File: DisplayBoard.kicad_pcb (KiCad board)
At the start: 4 copper layers, 35.6 x 38.2 mm, 42 parts, among them J201 Conn_Coaxial, J301 Conn_01x12_Pin, J401 Conn_01x04, Q301 L2N7002SLLT1G, U201 ESP32-S3-PICO-1-N8R2, U401 SN65HVD232, U501 USBLC6-2SC6, U502 AMS1117-3.3

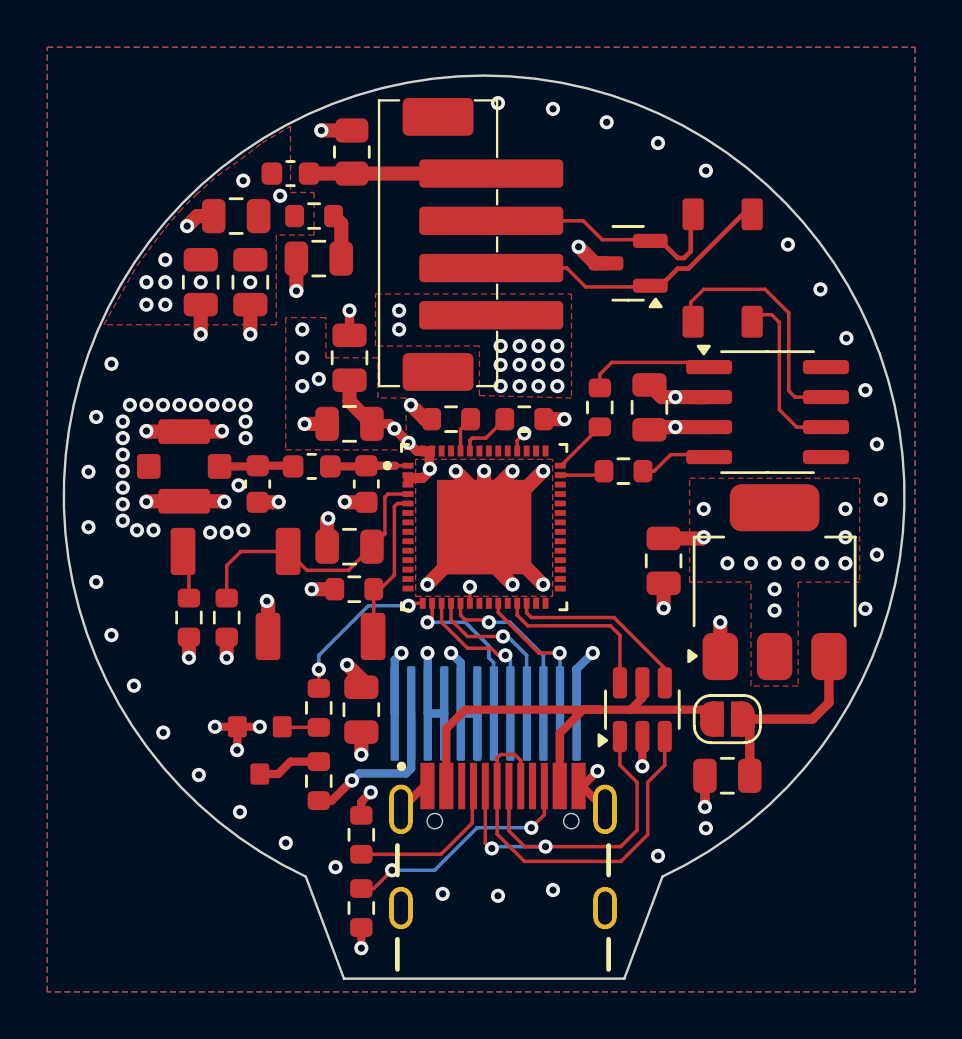
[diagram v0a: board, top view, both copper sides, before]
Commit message: Fixed wrong board outlines
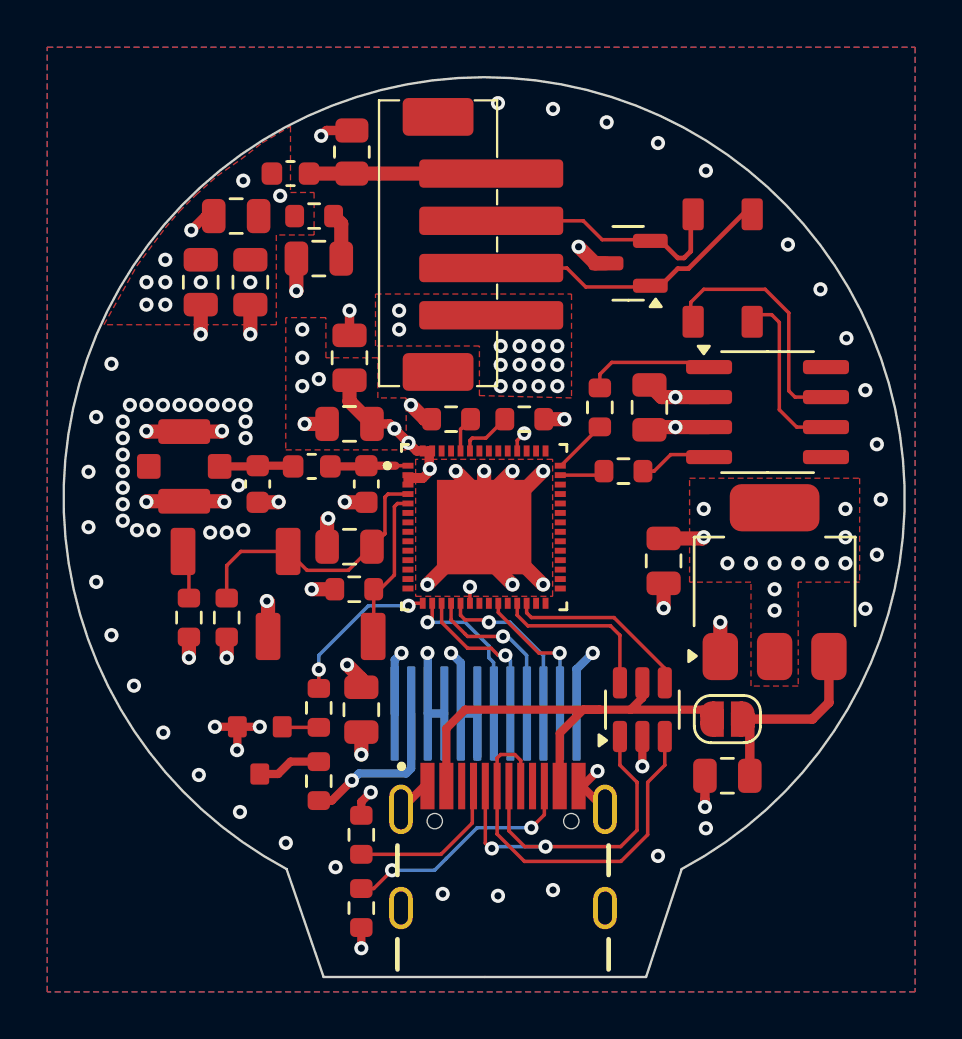
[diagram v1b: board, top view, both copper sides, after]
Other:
- board size 35.6 x 38.2 mm -> 35.6 x 38.1 mm
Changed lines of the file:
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@@
 		(embedded_fonts no)
 	)
+	(gr_line
+		(start 91.634396 133.548783)
+		(end 93.203009 138.119579)
+		(stroke
+			(width 0.1)
+			(type solid)
+		)
+		(layer "Edge.Cuts")
+	)
 	(gr_arc
-		(start 92.449248 133.869123)
-		(mid 100.000001 99.950001)
-		(end 107.55075 133.869124)
+		(start 91.634396 133.548783)
+		(mid 100 100.019548)
+		(end 108.365604 133.548783)
 		(stroke
 			(width 0.1)
@@
 	)
 	(gr_line
-		(start 94.06443 138.189125)
-		(end 105.935567 138.189126)
+		(start 106.858009 138.119579)
+		(end 108.365604 133.548783)
 		(stroke
 			(width 0.1)
@@
 	)
 	(gr_line
-		(start 92.449248 133.869123)
-		(end 94.06443 138.189125)
+		(start 100.033009 138.119579)
+		(end 106.858009 138.119579)
 		(stroke
 			(width 0.1)
@@
 	)
 	(gr_line
-		(start 107.55075 133.869124)
-		(end 105.935567 138.189126)
+		(start 100.033009 138.119579)
+		(end 93.203009 138.119579)
 		(stroke
 			(width 0.1)
@@
 	)
 	(segment
-		(start 87.848272 105.9)
-		(end 87.424641 106.323631)
-		(width 0.6)
-		(layer "F.Cu")
-		(net 1)
-	)
-	(segment
 		(start 100 119.069563)
 		(end 101.059563 119.069563)
@@
 	)
 	(segment
+		(start 94.4 102.275)
+		(end 93.325 102.275)
+		(width 0.4)
+		(layer "F.Cu")
+		(net 1)
+	)
+	(segment
 		(start 109.35 130.616687)
 		(end 109.352521 130.619208)
@@
 	)
 	(segment
-		(start 88.55 105.9)
-		(end 87.848272 105.9)
-		(width 0.6)
-		(layer "F.Cu")
-		(net 1)
-	)
-	(segment
 		(start 109.35 129.6)
 		(end 109.35 130.916687)
@@
 	)
 	(segment
-		(start 94.4 102.275)
-		(end 93.107902 102.275)
-		(width 0.6)
-		(layer "F.Cu")
-		(net 1)
-	)
-	(segment
 		(start 104.135 130.034999)
 		(end 105.120001 131.02)
@@
 	)
 	(segment
+		(start 93.325 102.275)
+		(end 93.1 102.5)
+		(width 0.4)
+		(layer "F.Cu")
+		(net 1)
+	)
+	(segment
 		(start 100 119.069563)
 		(end 100 119.1)
@@
 	)
 	(segment
-		(start 93.107902 102.275)
-		(end 93.107893 102.274991)
-		(width 0.6)
+		(start 88.55 105.9)
+		(end 88.2 105.9)
+		(width 0.4)
 		(layer "F.Cu")
 		(net 1)
@@
 	)
 	(segment
+		(start 88.2 105.9)
+		(end 87.6 106.5)
+		(width 0.4)
+		(layer "F.Cu")
+		(net 1)
+	)
+	(segment
 		(start 89.55 127.525)
 		(end 89.55 128.500995)
@@
 	)
 	(via
-		(at 85.7 113.9)
+		(at 87.6 106.5)
 		(size 0.6)
 		(drill 0.3)
@@
 	)
 	(via
-		(at 89.661103 131.133185)
+		(at 85.7 113.9)
 		(size 0.6)
 		(drill 0.3)
@@
 	)
 	(via
-		(at 87.424641 106.323631)
+		(at 89.661103 131.133185)
 		(size 0.6)
 		(drill 0.3)
@@
 	)
 	(via
+		(at 93.1 102.5)
+		(size 0.6)
+		(drill 0.3)
+		(layers "F.Cu" "B.Cu")
+		(net 1)
+	)
+	(via
 		(at 91.603423 132.443297)
 		(size 0.6)
@@
 	)
 	(via
-		(at 93.107893 102.274991)
-		(size 0.6)
-		(drill 0.3)
-		(layers "F.Cu" "B.Cu")
-		(net 1)
-	)
-	(via
 		(at 84.7 117.4)
 		(size 0.6)
@@
 	)
 	(group ""
-		(members "1408c1a9-8866-4fd6-90e4-1e7e4a77a13d" "884e87c2-7461-4ac5-aa46-83d93904fc0c"
-			"9a26e2bb-1390-4193-a48d-03b03680c98b" "b0379903-c7db-42f4-b03a-d2603a1ccc0a"
+		(members "13431fe7-04c9-4d11-b95e-dfc0e26d45e8" "151ce2fb-e82d-4c07-b562-dec3ba001190"
+			"3aeaa2b4-87d0-4c0e-915f-ef23df637329" "87ffcc5a-f92a-4349-a24a-bde821b8cdf3"
+			"ef0e61fd-4632-48e8-b592-595cd6067a15"
 		)
 	)

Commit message: Finished v1.1
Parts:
- removed C201: 1uF, Capacitor_SMD:C_0805_2012Metric
- removed C202, C502: 22uF, Capacitor_SMD:C_0805_2012Metric
- removed C203: 0.1uF, Capacitor_SMD:C_0805_2012Metric
- removed C204, C205: 3.3pF, Capacitor_SMD:C_0603_1608Metric
- removed C301: 104, Capacitor_SMD:C_0805_2012Metric
- removed C401, C402: unkwn, Capacitor_SMD:C_0805_2012Metric
- removed C403, C405: 100nF, Capacitor_SMD:C_0805_2012Metric
- removed C404: 47uF, Capacitor_SMD:C_0805_2012Metric
- removed C501: 10uF, Capacitor_SMD:C_0805_2012Metric
- removed D401: SP4020-01FTG-C, Resistor_SMD:R_0805_2012Metric
- removed D402: PESD1CAN, Package_TO_SOT_SMD:SOT-23
- removed FB401: BLM18KG121TN1D, Inductor_SMD:L_0603_1608Metric
- removed J201: Conn_Coaxial, CustomFootprints:CONMHF1-SMD-G-T_U.FL
- removed J401: Conn_01x04, CustomFootprints:JST_PH_B4B_SM4_TB
- removed JP501: SolderJumper_2_Open, Jumper:SolderJumper-2_P1.3mm_Open_RoundedPad1.0x1.5mm
- removed L201: 2.2nH, Inductor_SMD:L_0603_1608Metric
- removed L401: TDK ACT45B-510-2P-TL003, CustomFootprints:TDK ACT45B-510-2P-TL003
- removed Q301: L2N7002SLLT1G, CustomFootprints:SOT_TO_92_L2N7002SLLT1G
- removed R201: 470, Resistor_SMD:R_0603_1608Metric
- removed R202, R203, R205, R206: 10k, Resistor_SMD:R_0603_1608Metric
- removed R204, R402: 100, Resistor_SMD:R_0603_1608Metric
- removed R301: 1k, Resistor_SMD:R_0603_1608Metric
- removed R302: 10, Resistor_SMD:R_0603_1608Metric
- removed R401: 3, Resistor_SMD:R_0603_1608Metric
- removed RST201: SW_SPST, CustomFootprints:XUNPU_Button
- removed Rusb501, Rusb502: 5.1k, Resistor_SMD:R_0603_1608Metric
- removed SPST201: BOOT, CustomFootprints:XUNPU_Button
- removed U201: ESP32-S3-PICO-1-N8R2, CustomFootprints:ESP32-S3-PICO-1
- removed U401: SN65HVD232, Package_SO:SOIC-8_3.9x4.9mm_P1.27mm
- removed U501: USBLC6-2SC6, Package_TO_SOT_SMD:SOT-23-6
- removed U502: AMS1117-3.3, Package_TO_SOT_SMD:SOT-223-3_TabPin2
- removed USBC501: USB4105-GF-A, CustomFootprints:USB-C_24P-2.0
- added C1: 1uF, Capacitor_SMD:C_0805_2012Metric, F.Cu at (130.5, 129.9)
- added C10: 100nF, Capacitor_SMD:C_0805_2012Metric, F.Cu at (147.1, 104.4)
- added C11: 47uF, Capacitor_SMD:C_0805_2012Metric, F.Cu at (150.0, 108.2)
- added C12: 47uF, Capacitor_SMD:C_0805_2012Metric, F.Cu at (155.4, 109.7)
- added C13: 100nF, Capacitor_SMD:C_0805_2012Metric, F.Cu at (133.1, 112.7)
- added C14: 10uF, Capacitor_SMD:C_0805_2012Metric, F.Cu at (144.2, 128.7)
- added C15: 22uF, Capacitor_SMD:C_0805_2012Metric, F.Cu at (144.2, 132.2)
- added C2: 22uF, Capacitor_SMD:C_0805_2012Metric, F.Cu at (123.2, 126.8)
- added C3: 100nF, Capacitor_SMD:C_0805_2012Metric, F.Cu at (125.2, 126.8)
- added C4: 3.3pF, Capacitor_SMD:C_0603_1608Metric, F.Cu at (127.8, 132.5)
- added C5: 3.3pF, Capacitor_SMD:C_0603_1608Metric, F.Cu at (127.8, 127.8)
- added C6: 100nF, Capacitor_SMD:C_0805_2012Metric, F.Cu at (136.6, 116.0)
- added C7: 100nF, Capacitor_SMD:C_0805_2012Metric, F.Cu at (136.6, 113.8)
- added C8: unkwn, Capacitor_SMD:C_0805_2012Metric, F.Cu at (147.1, 102.2)
- added C9: unkwn, Capacitor_SMD:C_0805_2012Metric, F.Cu at (150.7, 103.4)
- added D1: SP4020-01FTG-C, Resistor_SMD:R_0805_2012Metric, F.Cu at (146.2, 107.5)
- added D2: PESD1CAN, Package_TO_SOT_SMD:SOT-23, F.Cu at (134.5, 105.0)
- added FB1: BLM18KG121TN1D, Inductor_SMD:L_0603_1608Metric, F.Cu at (148.0, 107.6)
- added J1: Conn_Coaxial, CustomFootprints:CONMHF1-SMD-G-T_U.FL, F.Cu at (131.8, 134.1)
- added J3: Conn_01x04, Connector_JST:JST_PH_B4B-PH-SM4-TB_1x04-1MP_P2.00mm_Vertical, F.Cu at (140.3, 105.0)
- added JP1: SolderJumper_2_Open, Jumper:SolderJumper-2_P1.3mm_Open_Pad1.0x1.5mm, F.Cu at (140.5, 127.1)
- added JP2: SolderJumper_2_Open, Jumper:SolderJumper-2_P1.3mm_Open_RoundedPad1.0x1.5mm, F.Cu at (143.6, 125.5)
- added L1: 2.2nH, Inductor_SMD:L_0603_1608Metric, F.Cu at (128.6, 130.1)
- added L2: TDK ACT45B-510-2P-TL003, CustomFootprints:TDK ACT45B-510-2P-TL003, F.Cu at (129.0, 105.0)
- added Q1: Si2302CDS-T1-GE3, Package_TO_SOT_SMD:SOT-23, F.Cu at (137.5, 127.0)
- added R1: 470, Resistor_SMD:R_0603_1608Metric, F.Cu at (135.3, 137.8)
- added R10: 3, Resistor_SMD:R_0603_1608Metric, F.Cu at (151.9, 106.6)
- added R11: 3, Resistor_SMD:R_0603_1608Metric, F.Cu at (153.5, 106.6)
- added R12: 100, Resistor_SMD:R_0603_1608Metric, F.Cu at (130.3, 116.3)
- added R2: 10k, Resistor_SMD:R_0603_1608Metric, F.Cu at (140.8, 132.5)
- added R3: 10k, Resistor_SMD:R_0603_1608Metric, F.Cu at (132.3, 129.8)
- added R4: 100, Resistor_SMD:R_0603_1608Metric, F.Cu at (127.3, 117.0)
- added R5: 10k, Resistor_SMD:R_0603_1608Metric, F.Cu at (125.3, 122.7)
- added R6: 10k, Resistor_SMD:R_0603_1608Metric, F.Cu at (125.3, 124.2)
- added R7: 10k, Resistor_SMD:R_0603_1608Metric, F.Cu at (137.0, 129.7)
- added R8: 100k, Resistor_SMD:R_0603_1608Metric, F.Cu at (140.3, 129.7)
- added R9: 10, Resistor_SMD:R_0603_1608Metric, F.Cu at (140.2, 124.6)
- added RST1: SW_SPST, CustomFootprints:XUNPU_Button, F.Cu at (136.2, 136.1)
- added Rusb1: 5.1k, Resistor_SMD:R_0603_1608Metric, F.Cu at (152.5, 123.7)
- added Rusb2: 5.1k, Resistor_SMD:R_0603_1608Metric, F.Cu at (152.5, 111.6)
- added SPST1: BOOT, CustomFootprints:XUNPU_Button, F.Cu at (138.8, 136.1)
- added U1: ESP32-S3-PICO-1-N8R2, CustomFootprints:ESP32-S3-PICO-1, F.Cu at (131.2, 123.1)
- added U2: SN65HVD232, Package_SO:SOIC-8_3.9x4.9mm_P1.27mm, F.Cu at (129.2, 110.9)
- added U3: USBLC6-2SC6, Package_TO_SOT_SMD:SOT-23-6, F.Cu at (145.3, 122.2)
- added U4: AMS1117-3.3, Package_TO_SOT_SMD:SOT-223-3_TabPin2, F.Cu at (149.2, 129.2)
- added USBC1: USB4105-GF-A, CustomFootprints:USB-C_24P-2.0, F.Cu at (155.9, 117.7)
- J2: renamed from J301; value Conn_01x12_Pin -> Conn_01x16; footprint CustomFootprints:GC9A01_Connector -> CustomFootprints:ST77916
- moved J2 44.3 mm to (139.5, 116.5), turned to 180 degrees
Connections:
- J2 pad 1: GND -> LEDK
- J2 pad 10: /MCU/DIN -> /Display/IO0
- J2 pad 11: /MCU/RST -> /Display/TE
- J2 pad 12: GND -> +3.3V
- J2 pad 2: LEDK -> +3.3V
- J2 pad 3: +3.3V -> GND
- J2 pad 4: +3.3V -> /Display/CS
- J2 pad 5: GND -> /Display/CLK
- J2 pad 6: GND -> /Display/RST
- J2 pad 7: /MCU/DC -> /Display/IO3
- J2 pad 8: /MCU/CS -> /Display/IO2
- J2 pad 9: /MCU/CLK -> /Display/IO1
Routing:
- net +3.3V: track 19.8 -> 47.7 mm, vias 35 -> 61
- net /Display/CS: track 0.00 -> 19.0 mm, vias 0 -> 1
- net /Display/RST: track 0.00 -> 16.4 mm, vias 0 -> 1
- net /Display/CLK: track 0.00 -> 15.6 mm, vias 0 -> 1
- net /Display/IO3: track 0.00 -> 15.1 mm, vias 0 -> 1
- net /Display/IO2: track 0.00 -> 11.7 mm, vias 0 -> 1
- net CANH: track 11.0 -> 0.00 mm
- net /Display/IO1: track 0.00 -> 10.9 mm, vias 0 -> 1
- net /Display/IO0: track 0.00 -> 10.0 mm, vias 0 -> 1
- net /Display/TE: track 0.00 -> 8.39 mm, vias 0 -> 1
- net CANL: track 7.36 -> 0.00 mm
- net CAN-: track 0.00 -> 7.25 mm
- net CAN+: track 0.00 -> 7.22 mm
- net /MCU/DIN: track 7.18 -> 0.00 mm, vias 1 -> 0
- net /MCU/BOOT: track 6.66 -> 13.8 mm
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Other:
- board size 35.6 x 38.1 mm -> 40.5 x 43.2 mm
- board text added: "1"
- board text added: "3.3V"
- board text added: "Boot"
- board text added: "C+"
- board text added: "C-"
- board text added: "EN"
- board text added: "GND"
- board text added: "LEDK"
- board text added: "LEDK LEDA GND CS CLK RST IO3 IO2 IO1 IO0 TE TCC GND GND GND"
- board text added: "VBUS"

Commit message: Silkscreen touchups & gerbers
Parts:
- J2: footprint CustomFootprints:ST77916 -> CustomFootprints:AFC01-S16FCC-00
- moved J2 2.55 mm to (139.5, 114.0)
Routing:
- net GND: track 78.7 -> 58.7 mm, vias 116 -> 117
- net +3.3V: track 47.7 -> 39.7 mm
- net /Display/CLK: track 15.6 -> 19.9 mm
- net /Display/CS: track 19.0 -> 22.9 mm
- net LEDK: track 9.42 -> 13.2 mm
- net /Display/IO2: track 11.7 -> 15.3 mm
- net /Display/IO1: track 10.9 -> 14.5 mm
- net /Display/IO0: track 10.0 -> 13.6 mm
- net /Display/RST: track 16.4 -> 19.6 mm
- net /Display/TE: track 8.39 -> 11.4 mm
- net /Display/IO3: track 15.1 -> 16.2 mm
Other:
- outline, holes or cut-outs redrawn
